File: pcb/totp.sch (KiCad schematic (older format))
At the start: 30 parts, among them J1 Conn_01x02, Q1 BSS84, Q2 BSS84, U1 ATmega32U4-AU, U2 MCP73831-2-OT, U3 AP2112K-3.3, U4 DS3231M, Y1 8MHz

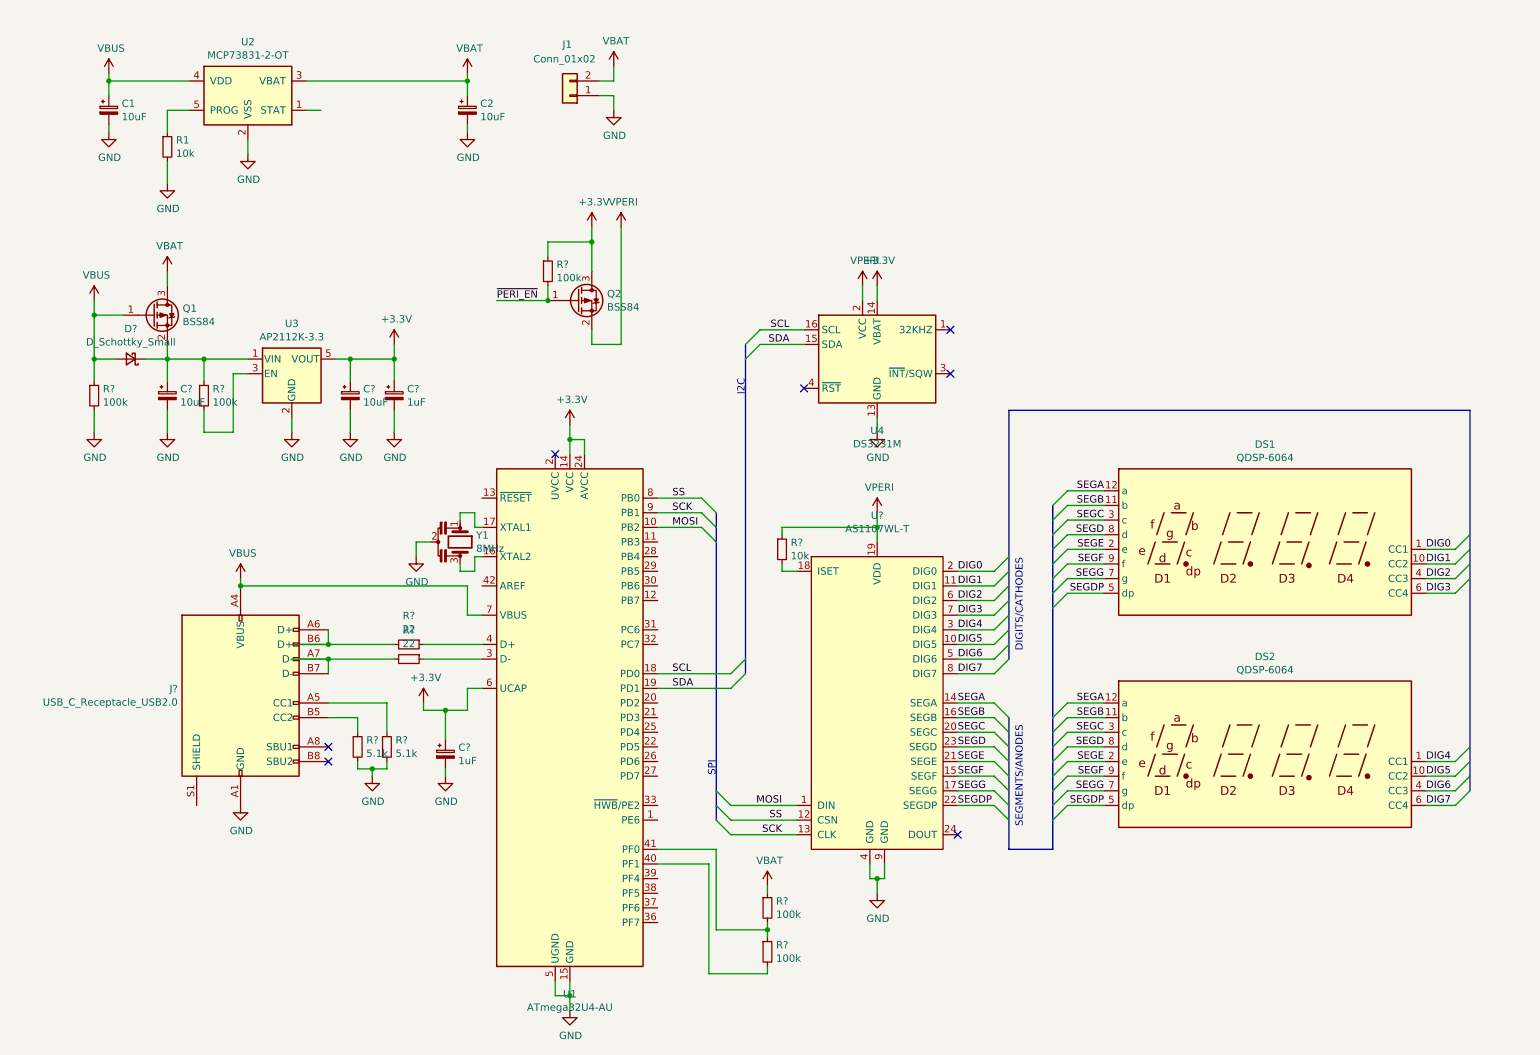
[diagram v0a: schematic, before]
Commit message: Update schematic (placement, swicth parts)
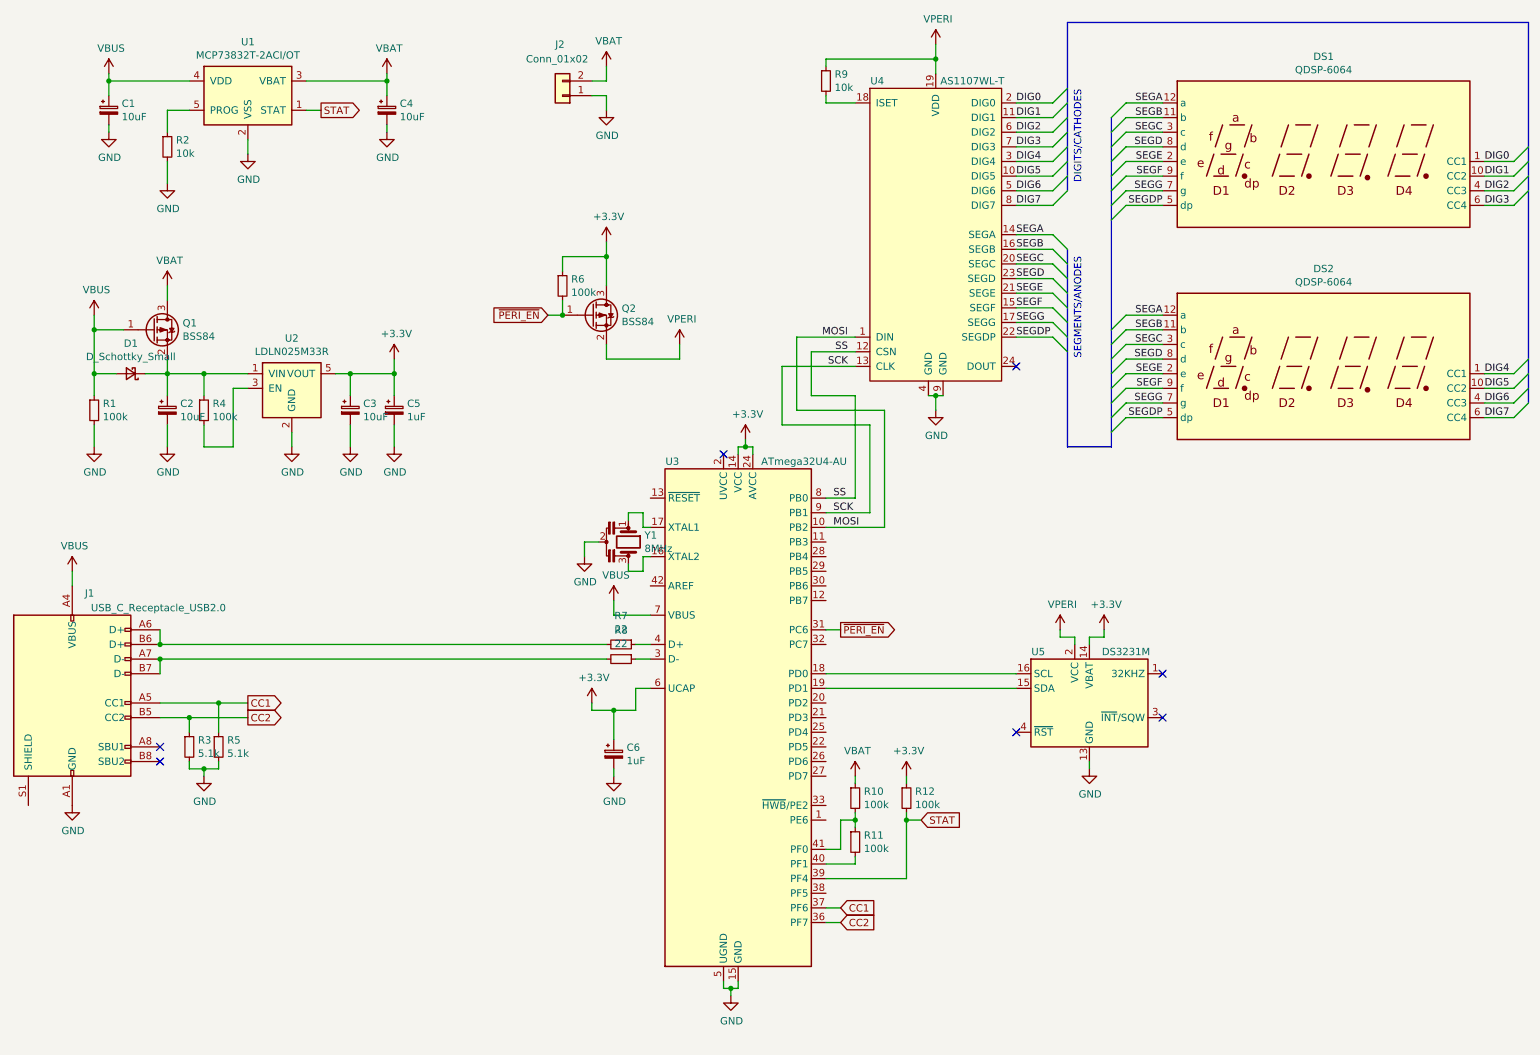
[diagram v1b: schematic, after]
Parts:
- removed U3: AP2112K-3.3, Package_TO_SOT_SMD:SOT-23-5, symbol Regulator_Linear:AP2112K-3.3
- added R12: 100k, symbol Device:R_Small
- added U2: LDLN025M33R, Package_TO_SOT_SMD:SOT-23-5, symbol totp:LDLN025M33R
- U1: renamed from U2; value MCP73831-2-OT -> MCP73832T-2ACI/OT
- gave numbers to parts that had none: 17
- renumbered C2 to C4, J1 to J2, R1 to R2, U1 to U3, U4 to U5
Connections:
- net +3V3: now also R12.1, U2.5 (VOUT)
- net GND: now also U2.2 (GND)
- net ~PERI_EN: now also U3.31 (PC6)
- net CC2: now reaches U3.36 (PF7)
- net CC2: now also J1.B5 (CC2), R3.1
- net CC1: now reaches U3.37 (PF6)
- net CC1: now also J1.A5 (CC1), R5.1
- net STAT: now reaches U3.39 (PF4)
- net STAT: now also U1.1 (STAT), R12.2
- net at C2.1, D1.1 (K), Q1.2 (S)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: now also U2.1 (VIN)
- net at R4.2: now also U2.3 (EN)
- net SCL: no longer names the net of U3.18 (PD0), U5.16 (SCL)
- net SDA: no longer names the net of U3.19 (PD1), U5.15 (SDA)
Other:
- note removed: "I2C"
- note removed: "SPI\n"
- moved on the sheet: C2, C3, C4, C5, C6, D1, DS1, DS2, J1, J2, Q1, Q2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

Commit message: Add MAX14636 symbol (charger detector)
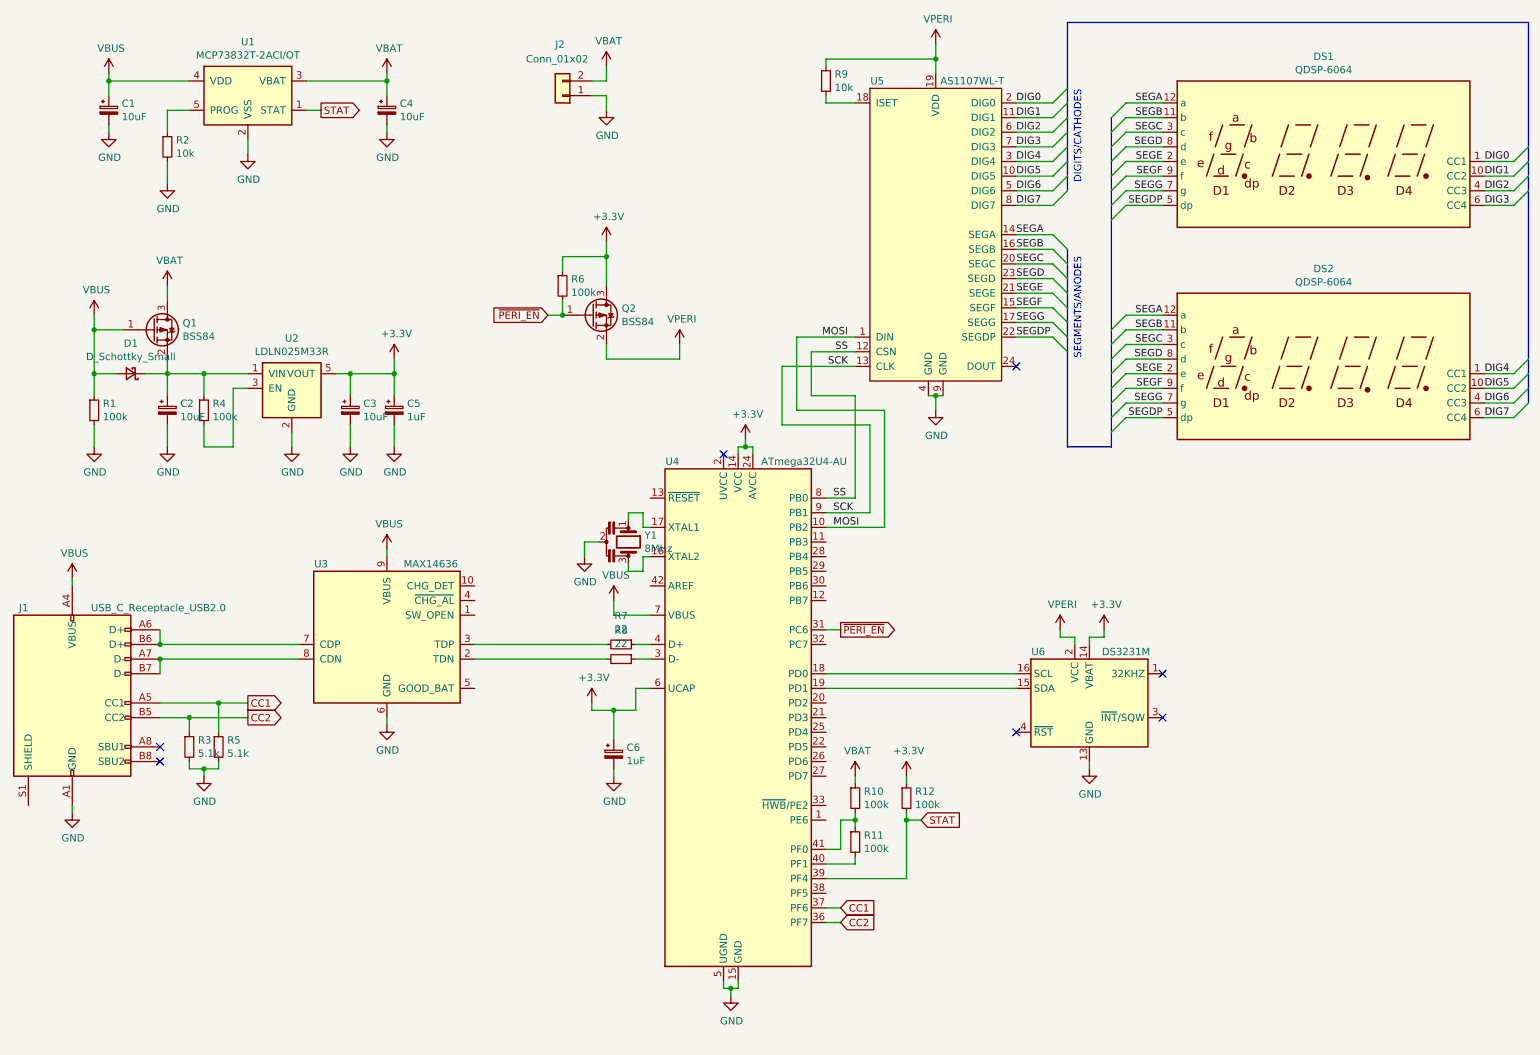
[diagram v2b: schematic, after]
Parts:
- added U3: MAX14636, symbol totp:MAX14636
- renumbered U3 to U4, U4 to U5, U5 to U6
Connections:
- net GND: now also U3.6 (GND)
- net VBUS: now also U3.9 (VBUS)
- net at J1.A6 (D+), J1.B6 (D+): now also U3.7 (CDP); no longer R7.2
- net at J1.A7 (D-), J1.B7 (D-): now also U3.8 (CDN); no longer R8.2
- new net: R7.2, U3.3 (TDP)
- new net: R8.2, U3.2 (TDN)
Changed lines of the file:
@@
 $EndDescr
 $Comp
-L Timer_RTC:DS3231M U5
+L Timer_RTC:DS3231M U6
 U 1 1 604BB822
 P 7950 5350
-F 0 "U5" H 7600 5700 50  0000 C CNN
+F 0 "U6" H 7600 5700 50  0000 C CNN
 F 1 "DS3231M" H 8200 5700 50  0000 C CNN
 F 2 "Package_SO:SOIC-16W_7.5x10.3mm_P1.27mm" H 7950 4750 50  0001 C CNN
@@
 $EndComp
 $Comp
-L power:+3.3V #PWR016
+L power:+3.3V #PWR018
 U 1 1 604CAA52
 P 3200 3000
-F 0 "#PWR016" H 3200 2850 50  0001 C CNN
+F 0 "#PWR018" H 3200 2850 50  0001 C CNN
 F 1 "+3.3V" H 3215 3173 50  0000 C CNN
 F 2 "" H 3200 3000 50  0001 C CNN
@@
 	2200 1600 2200 1500
 $Comp
-L power:GND #PWR022
+L power:GND #PWR023
 U 1 1 604CFC40
 P 4650 1300
-F 0 "#PWR022" H 4650 1050 50  0001 C CNN
+F 0 "#PWR023" H 4650 1050 50  0001 C CNN
 F 1 "GND" H 4655 1127 50  0000 C CNN
 F 2 "" H 4650 1300 50  0001 C CNN
@@
 	4650 1100 4550 1100
 $Comp
-L totp:VBAT #PWR021
+L totp:VBAT #PWR022
 U 1 1 604D537D
 P 4650 1000
-F 0 "#PWR021" H 4650 850 50  0001 C CNN
+F 0 "#PWR022" H 4650 850 50  0001 C CNN
 F 1 "VBAT" H 4665 1173 50  0000 C CNN
 F 2 "" H 4650 1000 50  0001 C CNN
@@
 $EndComp
 $Comp
-L power:GND #PWR017
+L power:GND #PWR019
 U 1 1 605815D6
 P 3200 3600
-F 0 "#PWR017" H 3200 3350 50  0001 C CNN
+F 0 "#PWR019" H 3200 3350 50  0001 C CNN
 F 1 "GND" H 3205 3427 50  0000 C CNN
 F 2 "" H 3200 3600 50  0001 C CNN
@@
 $EndComp
 $Comp
-L power:GND #PWR018
+L power:GND #PWR020
 U 1 1 60591DD5
 P 4500 4350
-F 0 "#PWR018" H 4500 4100 50  0001 C CNN
+F 0 "#PWR020" H 4500 4100 50  0001 C CNN
 F 1 "GND" H 4505 4177 50  0000 C CNN
 F 2 "" H 4500 4350 50  0001 C CNN
@@
 	4500 4250 4500 4350
 $Comp
-L power:+3.3V #PWR020
+L power:+3.3V #PWR021
 U 1 1 6059D76B
 P 4550 5350
-F 0 "#PWR020" H 4550 5200 50  0001 C CNN
+F 0 "#PWR021" H 4550 5200 50  0001 C CNN
 F 1 "+3.3V" H 4565 5523 50  0000 C CNN
 F 2 "" H 4550 5350 50  0001 C CNN
@@
 Connection ~ 1250 1100
 $Comp
-L power:GND #PWR033
+L power:GND #PWR035
 U 1 1 606518F9
 P 7950 5800
-F 0 "#PWR033" H 7950 5550 50  0001 C CNN
+F 0 "#PWR035" H 7950 5550 50  0001 C CNN
 F 1 "GND" H 7955 5627 50  0000 C CNN
 F 2 "" H 7950 5800 50  0001 C CNN
@@
 NoConn ~ 7450 3050
 $Comp
-L power:GND #PWR031
+L power:GND #PWR033
 U 1 1 60628E1A
 P 6900 3350
-F 0 "#PWR031" H 6900 3100 50  0001 C CNN
+F 0 "#PWR033" H 6900 3100 50  0001 C CNN
 F 1 "GND" H 6905 3177 50  0000 C CNN
 F 2 "" H 6900 3350 50  0001 C CNN
@@
 $EndComp
 $Comp
-L power:+3.3V #PWR019
+L power:+3.3V #PWR024
 U 1 1 6074A6E0
 P 4650 2200
-F 0 "#PWR019" H 4650 2050 50  0001 C CNN
+F 0 "#PWR024" H 4650 2050 50  0001 C CNN
 F 1 "+3.3V" H 4665 2373 50  0000 C CNN
 F 2 "" H 4650 2200 50  0001 C CNN
@@
 $EndComp
 $Comp
-L totp:VPERI #PWR025
+L totp:VPERI #PWR027
 U 1 1 6078A0D7
 P 5150 2900
-F 0 "#PWR025" H 5150 2750 50  0001 C CNN
+F 0 "#PWR027" H 5150 2750 50  0001 C CNN
 F 1 "VPERI" H 5165 3073 50  0000 C CNN
 F 2 "" H 5150 2900 50  0001 C CNN
@@
 Connection ~ 6900 950
 $Comp
-L totp:VPERI #PWR030
+L totp:VPERI #PWR032
 U 1 1 608E8A46
 P 6900 850
-F 0 "#PWR030" H 6900 700 50  0001 C CNN
+F 0 "#PWR032" H 6900 700 50  0001 C CNN
 F 1 "VPERI" H 6915 1023 50  0000 C CNN
 F 2 "" H 6900 850 50  0001 C CNN
@@
 L totp:VBUS #PWR01
 U 1 1 6059C5F9
-P 1000 4450
-F 0 "#PWR01" H 1000 4300 50  0001 C CNN
-F 1 "VBUS" H 1015 4623 50  0000 C CNN
-F 2 "" H 1000 4450 50  0001 C CNN
-F 3 "" H 1000 4450 50  0001 C CNN
-	1    1000 4450
+P 1000 4500
+F 0 "#PWR01" H 1000 4350 50  0001 C CNN
+F 1 "VBUS" H 1015 4673 50  0000 C CNN
+F 2 "" H 1000 4500 50  0001 C CNN
+F 3 "" H 1000 4500 50  0001 C CNN
+	1    1000 4500
 	1    0    0    -1
 $EndComp
@@
 L power:GND #PWR02
 U 1 1 604C71E8
-P 1000 6050
-F 0 "#PWR02" H 1000 5800 50  0001 C CNN
-F 1 "GND" H 1005 5877 50  0000 C CNN
-F 2 "" H 1000 6050 50  0001 C CNN
-F 3 "" H 1000 6050 50  0001 C CNN
-	1    1000 6050
+P 1000 6100
+F 0 "#PWR02" H 1000 5850 50  0001 C CNN
+F 1 "GND" H 1005 5927 50  0000 C CNN
+F 2 "" H 1000 6100 50  0001 C CNN
+F 3 "" H 1000 6100 50  0001 C CNN
+	1    1000 6100
 	1    0    0    -1
 $EndComp
@@
 U 1 1 60601BFE
 P 1000 5300
-F 0 "J1" H 1150 6000 50  0000 R CNN
+F 0 "J1" H 700 5900 50  0000 R CNN
 F 1 "USB_C_Receptacle_USB2.0" H 2050 5900 50  0000 R CNN
 F 2 "totp:USB_C_Receptacle_JAE_DX07S016JA1" H 1150 5800 50  0001 C CNN
@@
 	1    0    0    -1
 $EndComp
-Wire Wire Line
-	1000 4450 1000 4550
 $Comp
 L Device:R_Small R8
@@
 $EndComp
 $Comp
-L power:+3.3V #PWR027
+L power:+3.3V #PWR029
 U 1 1 604CC1DF
 P 5600 3550
-F 0 "#PWR027" H 5600 3400 50  0001 C CNN
+F 0 "#PWR029" H 5600 3400 50  0001 C CNN
 F 1 "+3.3V" H 5615 3723 50  0000 C CNN
 F 2 "" H 5600 3550 50  0001 C CNN
@@
 $EndComp
 $Comp
-L power:GND #PWR026
+L power:GND #PWR028
 U 1 1 604D7F91
 P 5500 7350
-F 0 "#PWR026" H 5500 7100 50  0001 C CNN
+F 0 "#PWR028" H 5500 7100 50  0001 C CNN
 F 1 "GND" H 5505 7177 50  0000 C CNN
 F 2 "" H 5500 7350 50  0001 C CNN
@@
 	4900 4150 4950 4150
 $Comp
-L power:GND #PWR024
+L power:GND #PWR026
 U 1 1 6059B137
 P 4700 5850
-F 0 "#PWR024" H 4700 5600 50  0001 C CNN
+F 0 "#PWR026" H 4700 5600 50  0001 C CNN
 F 1 "GND" H 4705 5677 50  0000 C CNN
 F 2 "" H 4700 5850 50  0001 C CNN
@@
 $EndComp
 $Comp
-L totp:VBAT #PWR028
+L totp:VBAT #PWR030
 U 1 1 60BCA18E
 P 6350 5850
-F 0 "#PWR028" H 6350 5700 50  0001 C CNN
+F 0 "#PWR030" H 6350 5700 50  0001 C CNN
 F 1 "VBAT" H 6365 6023 50  0000 C CNN
 F 2 "" H 6350 5850 50  0001 C CNN
@@
 	1600 5350 2000 5350
 $Comp
-L totp:VBUS #PWR023
+L totp:VBUS #PWR025
 U 1 1 607B7839
 P 4700 4650
-F 0 "#PWR023" H 4700 4500 50  0001 C CNN
+F 0 "#PWR025" H 4700 4500 50  0001 C CNN
 F 1 "VBUS" H 4715 4823 50  0000 C CNN
 F 2 "" H 4700 4650 50  0001 C CNN
@@
 	7800 3600 8100 3600
 $Comp
-L totp:AS1107WL-T U4
+L totp:AS1107WL-T U5
 U 1 1 6094A5B2
 P 6900 2150
-F 0 "U4" H 6500 3200 50  0000 C CNN
+F 0 "U5" H 6500 3200 50  0000 C CNN
 F 1 "AS1107WL-T" H 7150 3200 50  0000 C CNN
 F 2 "Package_SO:SOIC-24W_7.5x15.4mm_P1.27mm" H 6900 3700 50  0001 C CNN
@@
 	6150 5250 7450 5250
 Wire Wire Line
-	1600 5050 4650 5050
+	1600 5050 2550 5050
 Connection ~ 1600 5050
 Wire Wire Line
-	1600 4950 4650 4950
+	1600 4950 2550 4950
 Connection ~ 1600 4950
 Wire Wire Line
@@
 	6700 5850 6700 5900
 $Comp
-L power:+3.3V #PWR029
+L power:+3.3V #PWR031
 U 1 1 60920C13
 P 6700 5850
-F 0 "#PWR029" H 6700 5700 50  0001 C CNN
+F 0 "#PWR031" H 6700 5700 50  0001 C CNN
 F 1 "+3.3V" H 6715 6023 50  0000 C CNN
 F 2 "" H 6700 5850 50  0001 C CNN
@@
 	6150 6850 6250 6850
 $Comp
-L power:+3.3V #PWR034
+L power:+3.3V #PWR036
 U 1 1 60743670
 P 8050 4850
-F 0 "#PWR034" H 8050 4700 50  0001 C CNN
+F 0 "#PWR036" H 8050 4700 50  0001 C CNN
 F 1 "+3.3V" H 8065 5023 50  0000 C CNN
 F 2 "" H 8050 4850 50  0001 C CNN
@@
 $EndComp
 $Comp
-L totp:VPERI #PWR032
+L totp:VPERI #PWR034
 U 1 1 608E94C4
 P 7750 4850
-F 0 "#PWR032" H 7750 4700 50  0001 C CNN
+F 0 "#PWR034" H 7750 4700 50  0001 C CNN
 F 1 "VPERI" H 7765 5023 50  0000 C CNN
 F 2 "" H 7750 4850 50  0001 C CNN
@@
 	8050 4900 8050 4850
 $Comp
-L MCU_Microchip_ATmega:ATmega32U4-AU U3
+L MCU_Microchip_ATmega:ATmega32U4-AU U4
 U 1 1 603E7D30
 P 5550 5450
-F 0 "U3" H 5100 7200 50  0000 C CNN
+F 0 "U4" H 5100 7200 50  0000 C CNN
 F 1 "ATmega32U4-AU" H 6000 7200 50  0000 C CNN
 F 2 "Package_QFP:TQFP-44_10x10mm_P0.8mm" H 5550 5450 50  0001 C CIN
@@
 Wire Wire Line
 	4650 3000 5150 3000
+$Comp
+L totp:MAX14636 U3
+U 1 1 60C4FDEB
+P 3150 4850
+F 0 "U3" H 2700 5300 50  0000 C CNN
+F 1 "MAX14636" H 3450 5300 50  0000 C CNN
+F 2 "" H 3150 5900 50  0001 C CNN
+F 3 "https://datasheets.maximintegrated.com/en/ds/MAX14576-MAX14637.pdf" H 3000 6100 50  0001 C CNN
+	1    3150 4850
+	1    0    0    -1
+$EndComp
+Wire Wire Line
+	3750 5050 4650 5050
+Wire Wire Line
+	3750 4950 4650 4950
+$Comp
+L totp:VBUS #PWR016
+U 1 1 60C526B4
+P 3150 4300
+F 0 "#PWR016" H 3150 4150 50  0001 C CNN
+F 1 "VBUS" H 3165 4473 50  0000 C CNN
+F 2 "" H 3150 4300 50  0001 C CNN
+F 3 "" H 3150 4300 50  0001 C CNN
+	1    3150 4300
+	1    0    0    -1
+$EndComp
+Wire Wire Line
+	3150 4300 3150 4350
+Wire Wire Line
+	1000 6050 1000 6100
+$Comp
+L power:GND #PWR017
+U 1 1 60C882CB
+P 3150 5500
+F 0 "#PWR017" H 3150 5250 50  0001 C CNN
+F 1 "GND" H 3155 5327 50  0000 C CNN
+F 2 "" H 3150 5500 50  0001 C CNN
+F 3 "" H 3150 5500 50  0001 C CNN
+	1    3150 5500
+	1    0    0    -1
+$EndComp
+Wire Wire Line
+	3150 5500 3150 5450
+Wire Wire Line
+	1000 4500 1000 4550
 Wire Bus Line
 	10950 700  10950 3300
